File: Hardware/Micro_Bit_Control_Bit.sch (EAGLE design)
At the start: 38 parts, among them J1 Pokehome, J2 Pokehome, J3 Pokehome, J4 Pokehome, J5 Pokehome, J6 Pokehome, J7 Pokehome, J8 Pokehome, J9 QWIIC_RA, U2 micro:bit

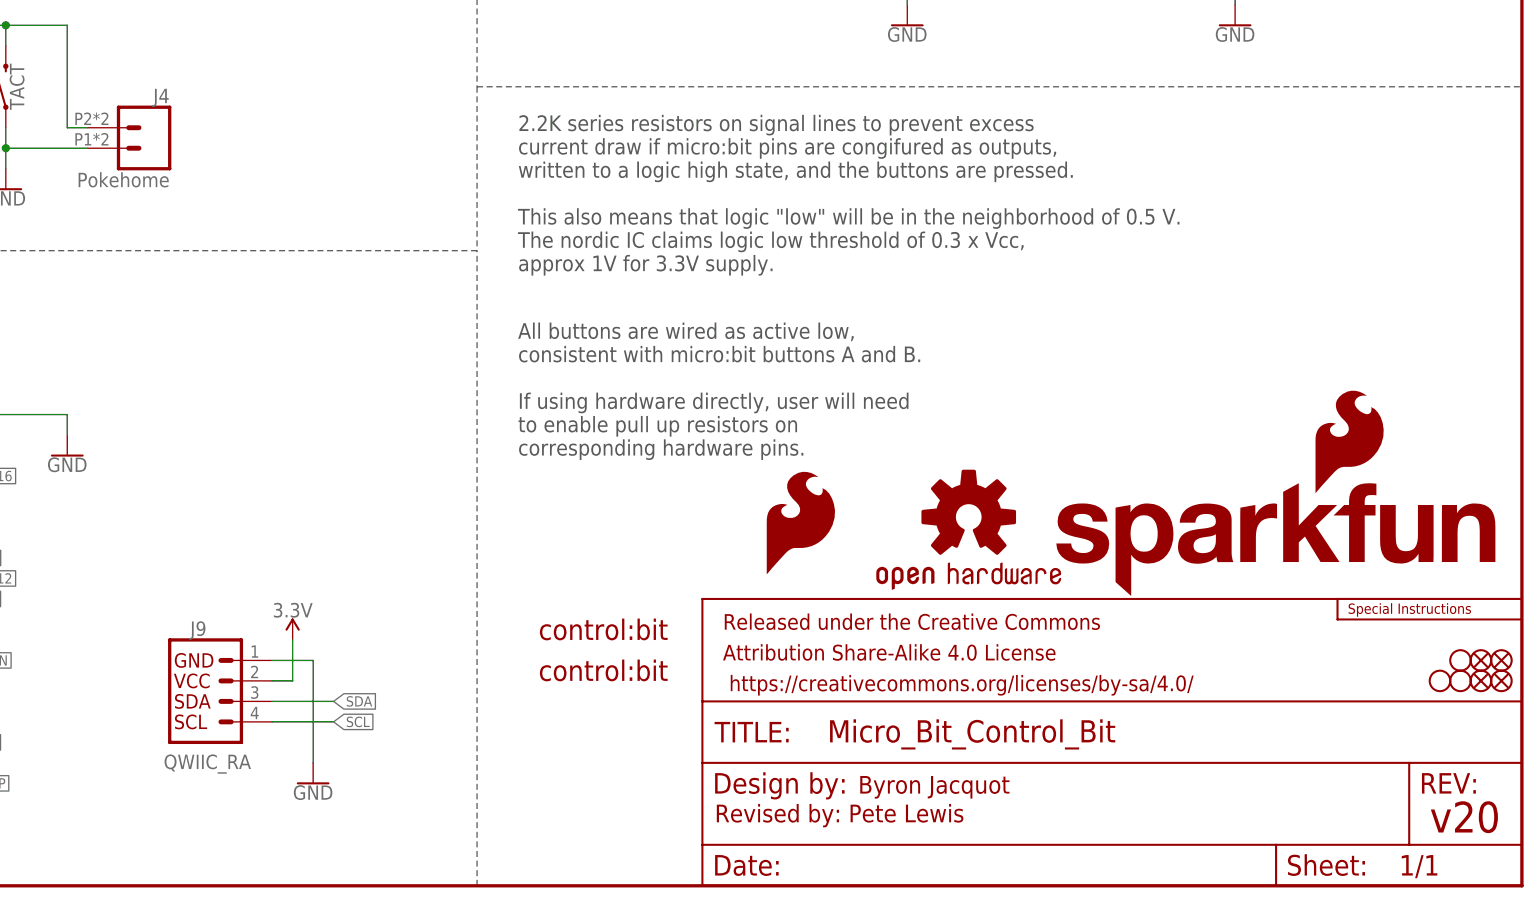
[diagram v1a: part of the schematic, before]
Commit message: Adding test points
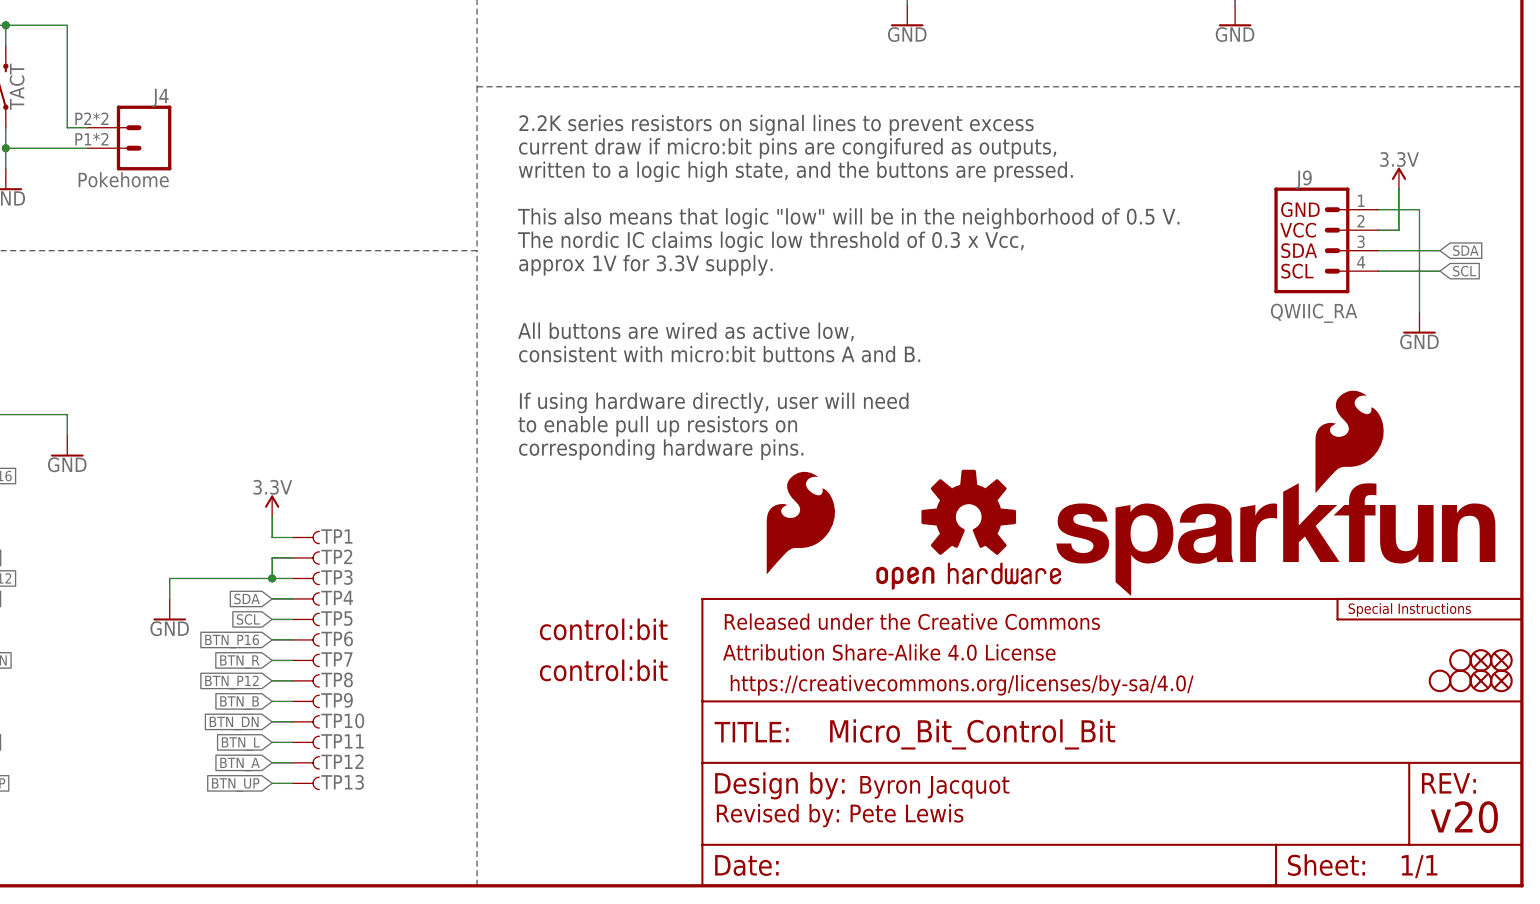
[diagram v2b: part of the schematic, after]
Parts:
- added TP1, TP10, TP11, TP12, TP13, TP2, TP3, TP4, TP5, TP6, TP7, TP8, TP9: TEST-POINT3, SparkFun-Connectors:TEST-POINT3
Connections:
- net 3.3V: now also TP1.1
- net BTN_A: now also TP12.1
- net BTN_B: now also TP9.1
- net BTN_DN: now also TP10.1
- net BTN_L: now also TP11.1
- net BTN_P12: now also TP8.1
- net BTN_P16: now also TP6.1
- net BTN_R: now also TP7.1
- net BTN_UP: now also TP13.1
- net GND: now also TP2.1, TP3.1
- net SCL: now also TP5.1
- net SDA: now also TP4.1
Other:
- moved on the sheet: J9
